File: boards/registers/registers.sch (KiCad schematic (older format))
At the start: 42 parts, among them U1 74ACT08, U2 74ACT244, U3 74AC273, U4 74ACT161

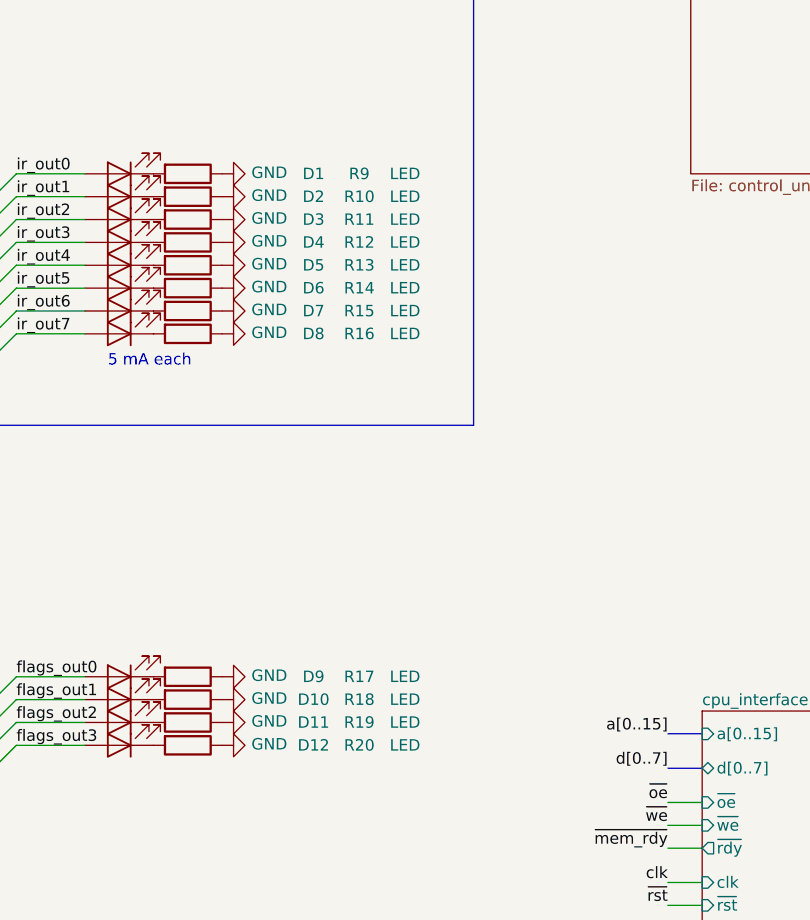
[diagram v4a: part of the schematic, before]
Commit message: LEDs and LED resistors
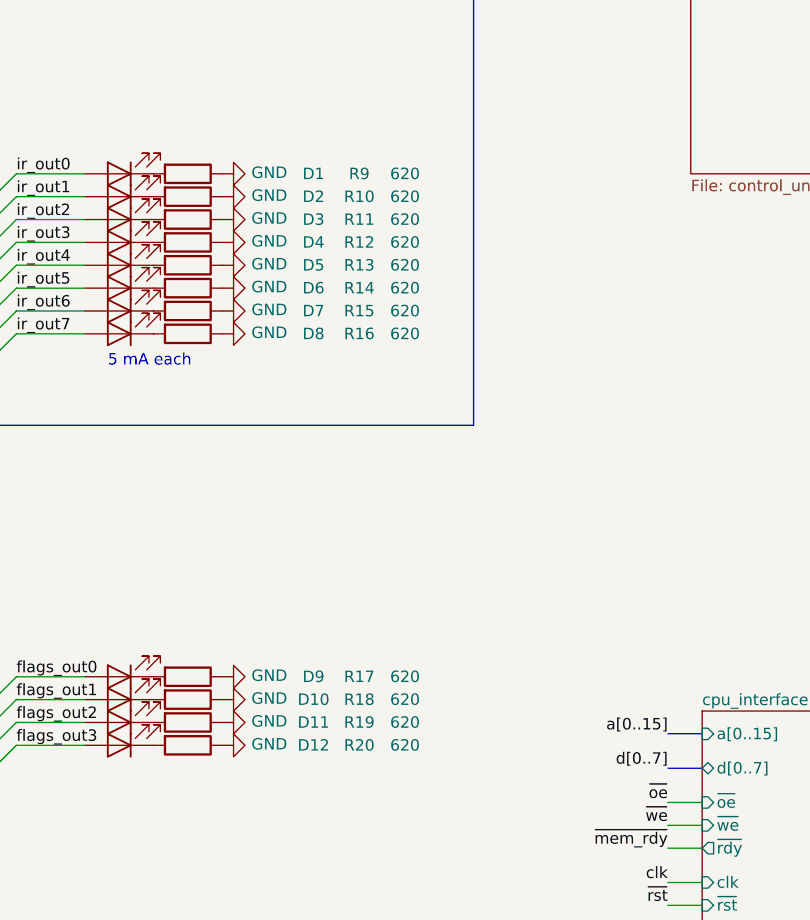
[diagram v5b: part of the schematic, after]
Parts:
- D1, D10, D11, D12, D2, D3, D4, D5, D6, D7, D8, D9: value LED -> KP-2012EC
- R10, R11, R12, R13, R14, R15, R16, R17, R18, R19, R20, R9: value LED -> 620
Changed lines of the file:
@@
 P 4950 5100
 F 0 "D1" H 4100 5100 50  0000 C CNN
-F 1 "LED" H 4943 4936 50  0001 C CNN
+F 1 "KP-2012EC" H 4943 4936 50  0001 C CNN
 F 2 "LED_SMD:LED_0805_2012Metric" H 4950 5100 50  0001 C CNN
 F 3 "~" H 4950 5100 50  0001 C CNN
@@
 P 5250 5100
 F 0 "R9" V 5250 5850 50  0000 C CNN
-F 1 "LED" V 5250 6050 50  0000 C CNN
+F 1 "620" V 5250 6050 50  0000 C CNN
 F 2 "Resistor_SMD:R_0805_2012Metric" V 5180 5100 50  0001 C CNN
 F 3 "~" H 5250 5100 50  0001 C CNN
@@
 P 4950 5200
 F 0 "D2" H 4100 5200 50  0000 C CNN
-F 1 "LED" H 4943 5036 50  0001 C CNN
+F 1 "KP-2012EC" H 4943 5036 50  0001 C CNN
 F 2 "LED_SMD:LED_0805_2012Metric" H 4950 5200 50  0001 C CNN
 F 3 "~" H 4950 5200 50  0001 C CNN
@@
 P 5250 5200
 F 0 "R10" V 5250 5950 50  0000 C CNN
-F 1 "LED" V 5250 6150 50  0000 C CNN
+F 1 "620" V 5250 6150 50  0000 C CNN
 F 2 "Resistor_SMD:R_0805_2012Metric" V 5180 5200 50  0001 C CNN
 F 3 "~" H 5250 5200 50  0001 C CNN
@@
 P 4950 5300
 F 0 "D3" H 4100 5300 50  0000 C CNN
-F 1 "LED" H 4943 5136 50  0001 C CNN
+F 1 "KP-2012EC" H 4943 5136 50  0001 C CNN
 F 2 "LED_SMD:LED_0805_2012Metric" H 4950 5300 50  0001 C CNN
 F 3 "~" H 4950 5300 50  0001 C CNN
@@
 P 5250 5300
 F 0 "R11" V 5250 6050 50  0000 C CNN
-F 1 "LED" V 5250 6250 50  0000 C CNN
+F 1 "620" V 5250 6250 50  0000 C CNN
 F 2 "Resistor_SMD:R_0805_2012Metric" V 5180 5300 50  0001 C CNN
 F 3 "~" H 5250 5300 50  0001 C CNN
@@
 P 4950 5400
 F 0 "D4" H 4100 5400 50  0000 C CNN
-F 1 "LED" H 4943 5236 50  0001 C CNN
+F 1 "KP-2012EC" H 4943 5236 50  0001 C CNN
 F 2 "LED_SMD:LED_0805_2012Metric" H 4950 5400 50  0001 C CNN
 F 3 "~" H 4950 5400 50  0001 C CNN
@@
 P 5250 5400
 F 0 "R12" V 5250 6150 50  0000 C CNN
-F 1 "LED" V 5250 6350 50  0000 C CNN
+F 1 "620" V 5250 6350 50  0000 C CNN
 F 2 "Resistor_SMD:R_0805_2012Metric" V 5180 5400 50  0001 C CNN
 F 3 "~" H 5250 5400 50  0001 C CNN
@@
 P 4950 5500
 F 0 "D5" H 4100 5500 50  0000 C CNN
-F 1 "LED" H 4943 5336 50  0001 C CNN
+F 1 "KP-2012EC" H 4943 5336 50  0001 C CNN
 F 2 "LED_SMD:LED_0805_2012Metric" H 4950 5500 50  0001 C CNN
 F 3 "~" H 4950 5500 50  0001 C CNN
@@
 P 5250 5500
 F 0 "R13" V 5250 6250 50  0000 C CNN
-F 1 "LED" V 5250 6450 50  0000 C CNN
+F 1 "620" V 5250 6450 50  0000 C CNN
 F 2 "Resistor_SMD:R_0805_2012Metric" V 5180 5500 50  0001 C CNN
 F 3 "~" H 5250 5500 50  0001 C CNN
@@
 P 4950 5600
 F 0 "D6" H 4100 5600 50  0000 C CNN
-F 1 "LED" H 4943 5436 50  0001 C CNN
+F 1 "KP-2012EC" H 4943 5436 50  0001 C CNN
 F 2 "LED_SMD:LED_0805_2012Metric" H 4950 5600 50  0001 C CNN
 F 3 "~" H 4950 5600 50  0001 C CNN
@@
 P 5250 5600
 F 0 "R14" V 5250 6350 50  0000 C CNN
-F 1 "LED" V 5250 6550 50  0000 C CNN
+F 1 "620" V 5250 6550 50  0000 C CNN
 F 2 "Resistor_SMD:R_0805_2012Metric" V 5180 5600 50  0001 C CNN
 F 3 "~" H 5250 5600 50  0001 C CNN
@@
 P 4950 5700
 F 0 "D7" H 4100 5700 50  0000 C CNN
-F 1 "LED" H 4943 5536 50  0001 C CNN
+F 1 "KP-2012EC" H 4943 5536 50  0001 C CNN
 F 2 "LED_SMD:LED_0805_2012Metric" H 4950 5700 50  0001 C CNN
 F 3 "~" H 4950 5700 50  0001 C CNN
@@
 P 5250 5700
 F 0 "R15" V 5250 6450 50  0000 C CNN
-F 1 "LED" V 5250 6650 50  0000 C CNN
+F 1 "620" V 5250 6650 50  0000 C CNN
 F 2 "Resistor_SMD:R_0805_2012Metric" V 5180 5700 50  0001 C CNN
 F 3 "~" H 5250 5700 50  0001 C CNN
@@
 P 4950 5800
 F 0 "D8" H 4100 5800 50  0000 C CNN
-F 1 "LED" H 4943 5636 50  0001 C CNN
+F 1 "KP-2012EC" H 4943 5636 50  0001 C CNN
 F 2 "LED_SMD:LED_0805_2012Metric" H 4950 5800 50  0001 C CNN
 F 3 "~" H 4950 5800 50  0001 C CNN
@@
 P 5250 5800
 F 0 "R16" V 5250 6550 50  0000 C CNN
-F 1 "LED" V 5250 6750 50  0000 C CNN
+F 1 "620" V 5250 6750 50  0000 C CNN
 F 2 "Resistor_SMD:R_0805_2012Metric" V 5180 5800 50  0001 C CNN
 F 3 "~" H 5250 5800 50  0001 C CNN
@@
 P 4950 7300
 F 0 "D9" H 4100 7300 50  0000 C CNN
-F 1 "LED" H 4943 7136 50  0001 C CNN
+F 1 "KP-2012EC" H 4943 7136 50  0001 C CNN
 F 2 "LED_SMD:LED_0805_2012Metric" H 4950 7300 50  0001 C CNN
 F 3 "~" H 4950 7300 50  0001 C CNN
@@
 P 5250 7300
 F 0 "R17" V 5250 8050 50  0000 C CNN
-F 1 "LED" V 5250 8250 50  0000 C CNN
+F 1 "620" V 5250 8250 50  0000 C CNN
 F 2 "Resistor_SMD:R_0805_2012Metric" V 5180 7300 50  0001 C CNN
 F 3 "~" H 5250 7300 50  0001 C CNN
@@
 P 4950 7400
 F 0 "D10" H 4100 7400 50  0000 C CNN
-F 1 "LED" H 4943 7236 50  0001 C CNN
+F 1 "KP-2012EC" H 4943 7236 50  0001 C CNN
 F 2 "LED_SMD:LED_0805_2012Metric" H 4950 7400 50  0001 C CNN
 F 3 "~" H 4950 7400 50  0001 C CNN
@@
 P 5250 7400
 F 0 "R18" V 5250 8150 50  0000 C CNN
-F 1 "LED" V 5250 8350 50  0000 C CNN
+F 1 "620" V 5250 8350 50  0000 C CNN
 F 2 "Resistor_SMD:R_0805_2012Metric" V 5180 7400 50  0001 C CNN
 F 3 "~" H 5250 7400 50  0001 C CNN
@@
 P 4950 7500
 F 0 "D11" H 4100 7500 50  0000 C CNN
-F 1 "LED" H 4943 7336 50  0001 C CNN
+F 1 "KP-2012EC" H 4943 7336 50  0001 C CNN
 F 2 "LED_SMD:LED_0805_2012Metric" H 4950 7500 50  0001 C CNN
 F 3 "~" H 4950 7500 50  0001 C CNN
@@
 P 5250 7500
 F 0 "R19" V 5250 8250 50  0000 C CNN
-F 1 "LED" V 5250 8450 50  0000 C CNN
+F 1 "620" V 5250 8450 50  0000 C CNN
 F 2 "Resistor_SMD:R_0805_2012Metric" V 5180 7500 50  0001 C CNN
 F 3 "~" H 5250 7500 50  0001 C CNN
@@
 P 4950 7600
 F 0 "D12" H 4100 7600 50  0000 C CNN
-F 1 "LED" H 4943 7436 50  0001 C CNN
+F 1 "KP-2012EC" H 4943 7436 50  0001 C CNN
 F 2 "LED_SMD:LED_0805_2012Metric" H 4950 7600 50  0001 C CNN
 F 3 "~" H 4950 7600 50  0001 C CNN
@@
 P 5250 7600
 F 0 "R20" V 5250 8350 50  0000 C CNN
-F 1 "LED" V 5250 8550 50  0000 C CNN
+F 1 "620" V 5250 8550 50  0000 C CNN
 F 2 "Resistor_SMD:R_0805_2012Metric" V 5180 7600 50  0001 C CNN
 F 3 "~" H 5250 7600 50  0001 C CNN

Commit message: Part names
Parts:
- U1: value 74ACT08 -> SN74ACT08PW
- U2: value 74ACT244 -> SN74ACT244PW
- U3: value 74AC273 -> MC74AC273DTR2G
- U4: value 74ACT161 -> MC74ACT161DG
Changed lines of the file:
@@
 P 3350 4150
 F 0 "U3" H 3750 3600 50  0000 C CNN
-F 1 "74AC273" H 3800 3500 50  0000 C CNN
+F 1 "MC74AC273DTR2G" H 3800 3500 50  0000 C CNN
 F 2 "Package_SO:TSSOP-20_4.4x6.5mm_P0.65mm" H 3350 4150 50  0001 C CNN
 F 3 "https://assets.nexperia.com/documents/data-sheet/74HC_HCT273.pdf" H 3350 4150 50  0001 C CNN
@@
 P 3350 1550
 F 0 "U2" H 3750 1000 50  0000 C CNN
-F 1 "74ACT244" H 3650 900 50  0000 C CNN
+F 1 "SN74ACT244PW" H 3650 900 50  0000 C CNN
 F 2 "Package_SO:TSSOP-20_4.4x6.5mm_P0.65mm" H 3350 1550 50  0001 C CNN
 F 3 "https://assets.nexperia.com/documents/data-sheet/74HC_HCT244.pdf" H 3350 1550 50  0001 C CNN
@@
 P 2100 5350
 F 0 "U1" H 2100 5675 50  0000 C CNN
-F 1 "74ACT08" H 2100 5584 50  0000 C CNN
+F 1 "SN74ACT08PW" H 2100 5584 50  0000 C CNN
 F 2 "Package_SO:TSSOP-14_4.4x5mm_P0.65mm" H 2100 5350 50  0001 C CNN
 F 3 "http://www.ti.com/lit/gpn/sn74LS08" H 2100 5350 50  0001 C CNN
@@
 P 10300 3450
 F 0 "U1" H 10300 3775 50  0000 C CNN
-F 1 "74ACT08" H 10300 3684 50  0000 C CNN
+F 1 "SN74ACT08PW" H 10300 3684 50  0000 C CNN
 F 2 "Package_SO:TSSOP-14_4.4x5mm_P0.65mm" H 10300 3450 50  0001 C CNN
 F 3 "http://www.ti.com/lit/gpn/sn74LS08" H 10300 3450 50  0001 C CNN
@@
 P 10300 5050
 F 0 "U1" H 10300 5375 50  0000 C CNN
-F 1 "74ACT08" H 10300 5284 50  0000 C CNN
+F 1 "SN74ACT08PW" H 10300 5284 50  0000 C CNN
 F 2 "Package_SO:TSSOP-14_4.4x5mm_P0.65mm" H 10300 5050 50  0001 C CNN
 F 3 "http://www.ti.com/lit/gpn/sn74LS08" H 10300 5050 50  0001 C CNN
@@
 P 1000 10500
 F 0 "U1" H 1230 10546 50  0000 L CNN
-F 1 "74ACT08" H 1230 10455 50  0000 L CNN
+F 1 "SN74ACT08PW" H 1230 10455 50  0000 L CNN
 F 2 "Package_SO:TSSOP-14_4.4x5mm_P0.65mm" H 1000 10500 50  0001 C CNN
 F 3 "http://www.ti.com/lit/gpn/sn74LS08" H 1000 10500 50  0001 C CNN
@@
 P 3350 6800
 F 0 "U4" H 3750 6250 50  0000 C CNN
-F 1 "74ACT161" H 3650 6150 50  0000 C CNN
+F 1 "MC74ACT161DG" H 3650 6150 50  0000 C CNN
 F 2 "Package_SO:SOIC-16_3.9x9.9mm_P1.27mm" H 3350 6800 50  0001 C CNN
 F 3 "http://www.ti.com/lit/gpn/sn74LS161" H 3350 6800 50  0001 C CNN
@@
 P 2650 10600
 F 0 "U1" H 2650 10925 50  0000 C CNN
-F 1 "74ACT08" H 2650 10834 50  0000 C CNN
+F 1 "SN74ACT08PW" H 2650 10834 50  0000 C CNN
 F 2 "Package_SO:TSSOP-14_4.4x5mm_P0.65mm" H 2650 10600 50  0001 C CNN
 F 3 "http://www.ti.com/lit/gpn/sn74LS08" H 2650 10600 50  0001 C CNN
